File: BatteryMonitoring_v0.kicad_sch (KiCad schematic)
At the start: 33 parts, among them J10 Conn_01x05_Pin, J7 Conn_01x03_Pin, J8 Conn_01x05_Pin, J9 Conn_01x06_Pin, Q6 NPN, SW3 RST_SHUT, SW4 WAKE, U2 PBQ76952PFBT

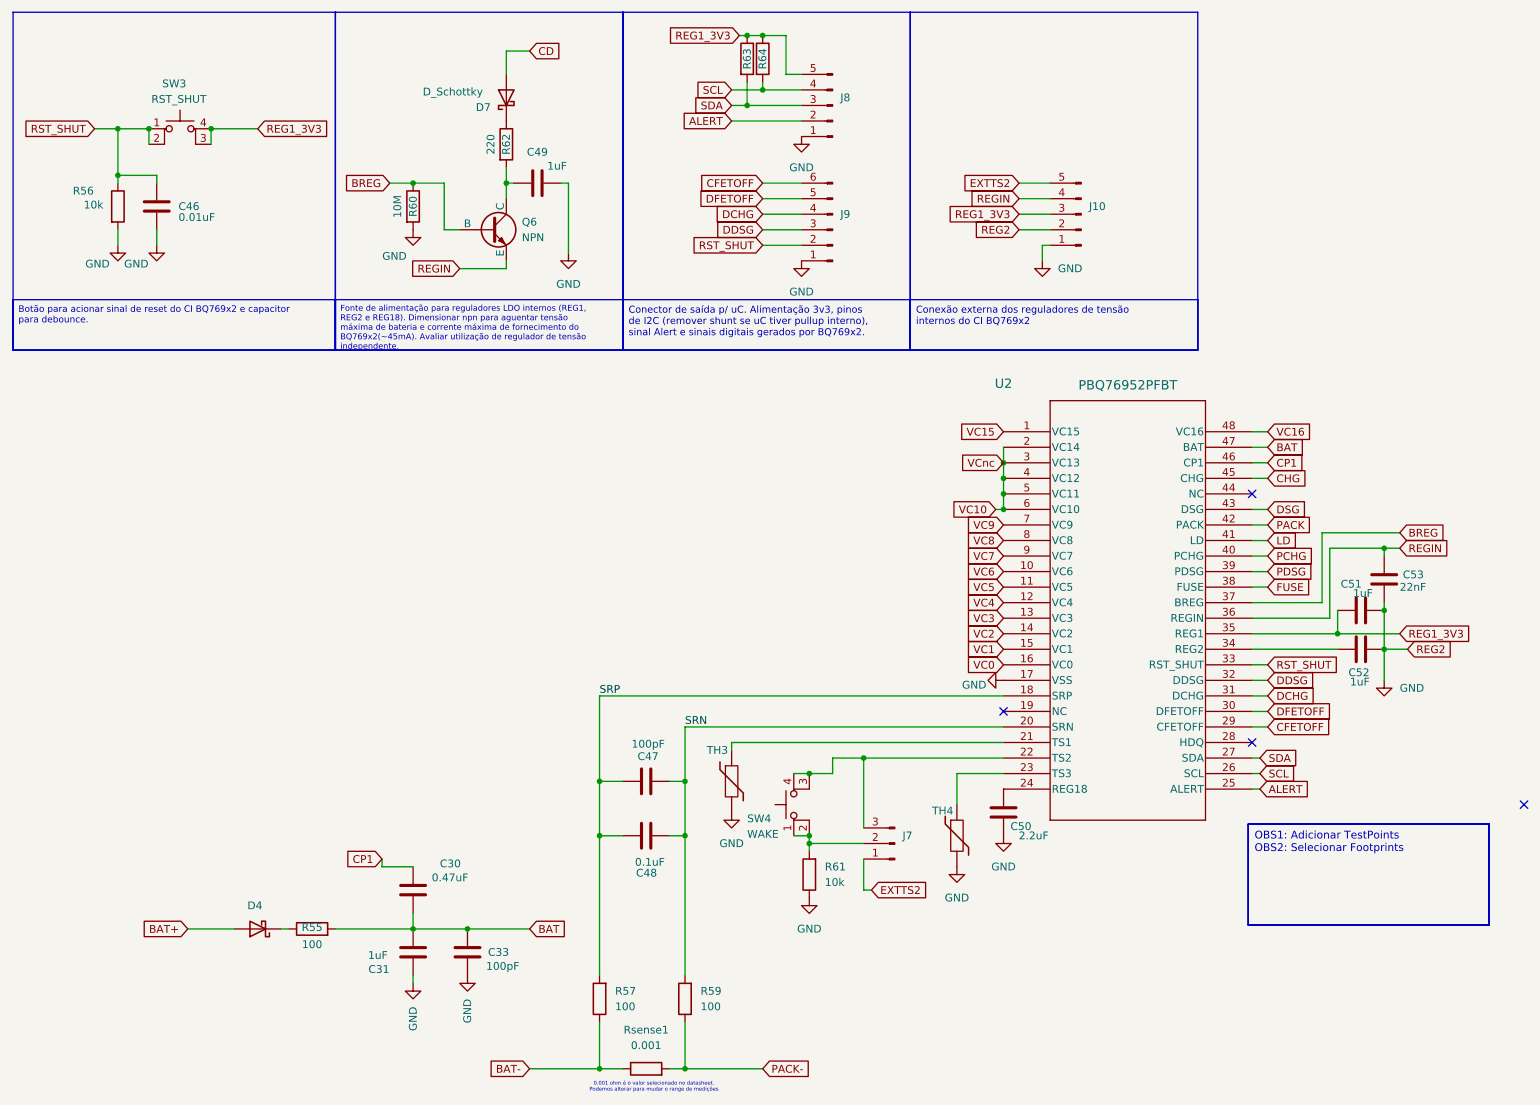
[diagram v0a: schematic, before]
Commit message: Inicio do roteamento e posicionamento da PCB
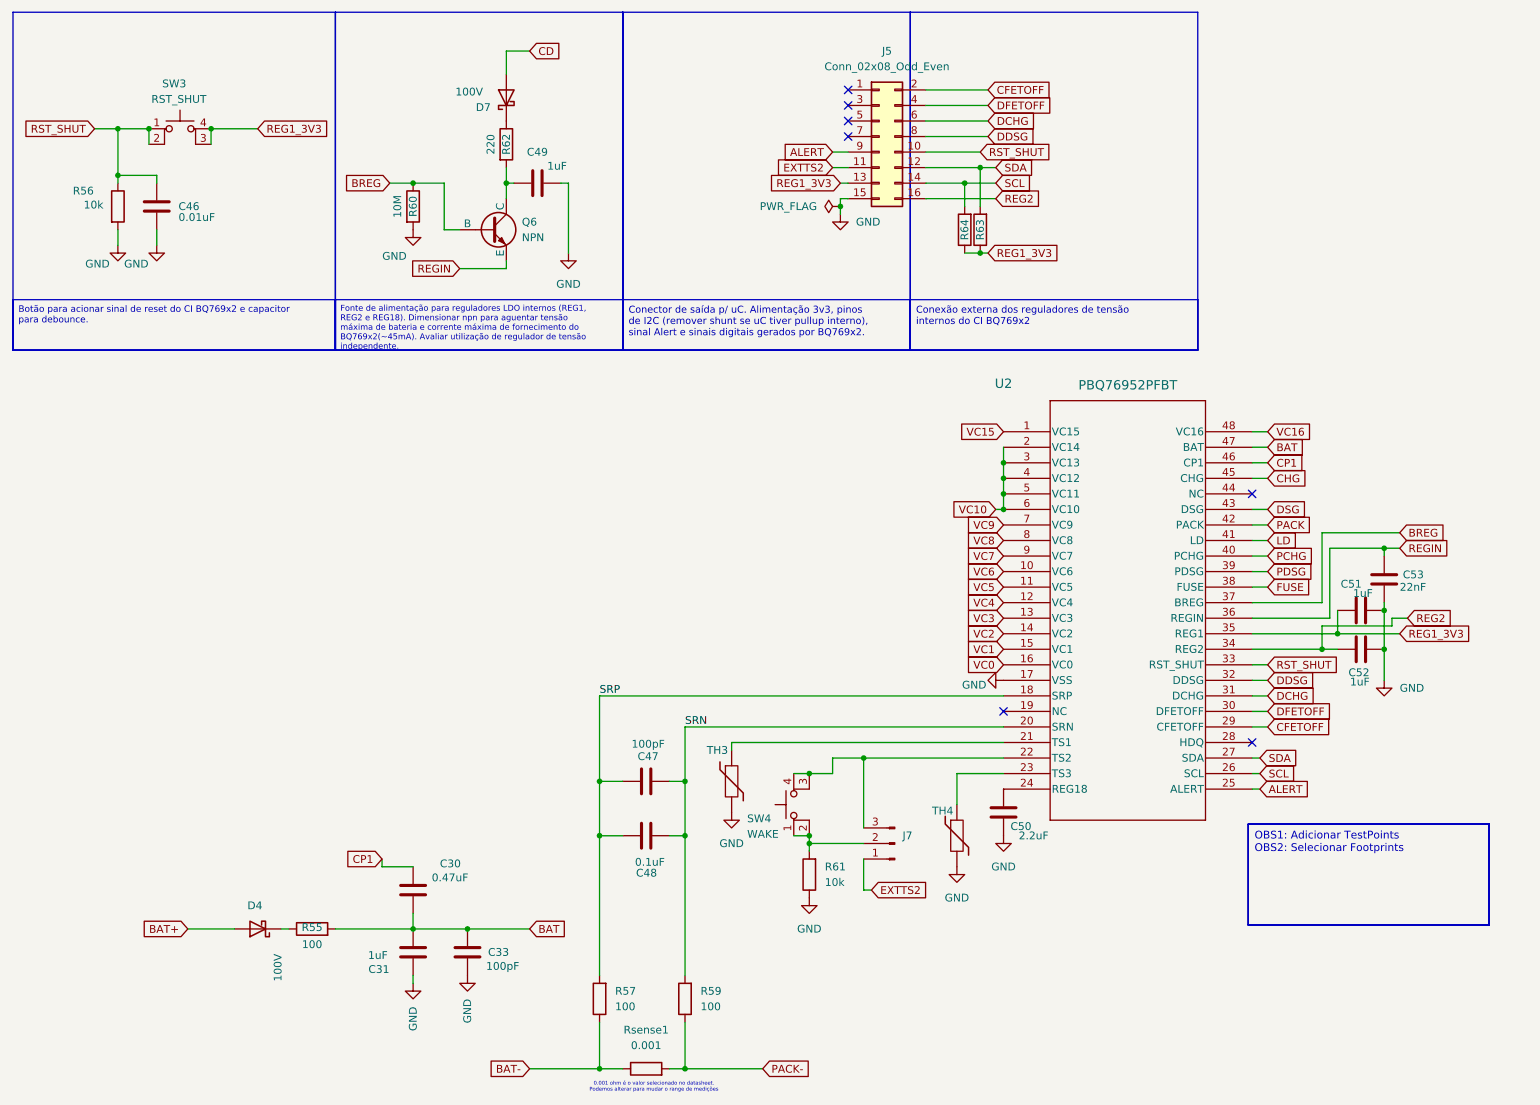
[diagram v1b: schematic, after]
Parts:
- removed J10, J8: Conn_01x05_Pin, Connector_PinHeader_2.54mm:PinHeader_1x05_P2.54mm_Vertical, symbol Connector:Conn_01x05_Pin
- removed J9: Conn_01x06_Pin, Connector_PinHeader_2.54mm:PinHeader_1x06_P2.54mm_Vertical, symbol Connector:Conn_01x06_Pin
- added J5: Conn_02x08_Odd_Even, Connector_PinHeader_2.54mm:PinHeader_2x08_P2.54mm_Vertical, symbol Connector_Generic:Conn_02x08_Odd_Even
- C30, C31, C33, C46, C47, C48, C49, C50, C51, C52, C53: footprint Capacitor_SMD:C_0402_1005Metric_Pad0.74x0.62mm_HandSolder -> Capacitor_SMD:C_1206_3216Metric_Pad1.33x1.80mm_HandSolder
- D4, D7: value D_Schottky -> 100V
- Q6: footprint Package_TO_SOT_SMD:SOT-89-3 -> Package_TO_SOT_THT:TO-92
- R55, R56, R57, R59, R60, R61, R62, R63, R64: footprint Resistor_SMD:R_0402_1005Metric -> Resistor_SMD:R_1206_3216Metric
- TH3, TH4: footprint Footprints:103AT2 -> footprints:103AT2
- U2: footprint Footprints:BQ76952_TEX -> footprints:BQ7692_TEX
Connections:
- net ALERT: now also J5.9 (Pin_9)
- net CFETOFF: now also J5.2 (Pin_2)
- net DCHG: now also J5.6 (Pin_6)
- net DDSG: now also J5.8 (Pin_8)
- net DFETOFF: now also J5.4 (Pin_4)
- net EXTTS2: now also J5.11 (Pin_11)
- net GND: now also J5.15 (Pin_15)
- net REG1_3V3: now also J5.13 (Pin_13)
- net RST_SHUT: now also J5.10 (Pin_10)
- net SCL: now also J5.14 (Pin_14)
- net SDA: now also J5.12 (Pin_12)
- net REG2: now reaches C52.2, U2.34 (REG2)
- net REG2: now also J5.16 (Pin_16)
- no-connect marks 4 -> 7
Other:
- moved on the sheet: R63, R64

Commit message: add Res Shunt e atualiza para Kicad 9.0
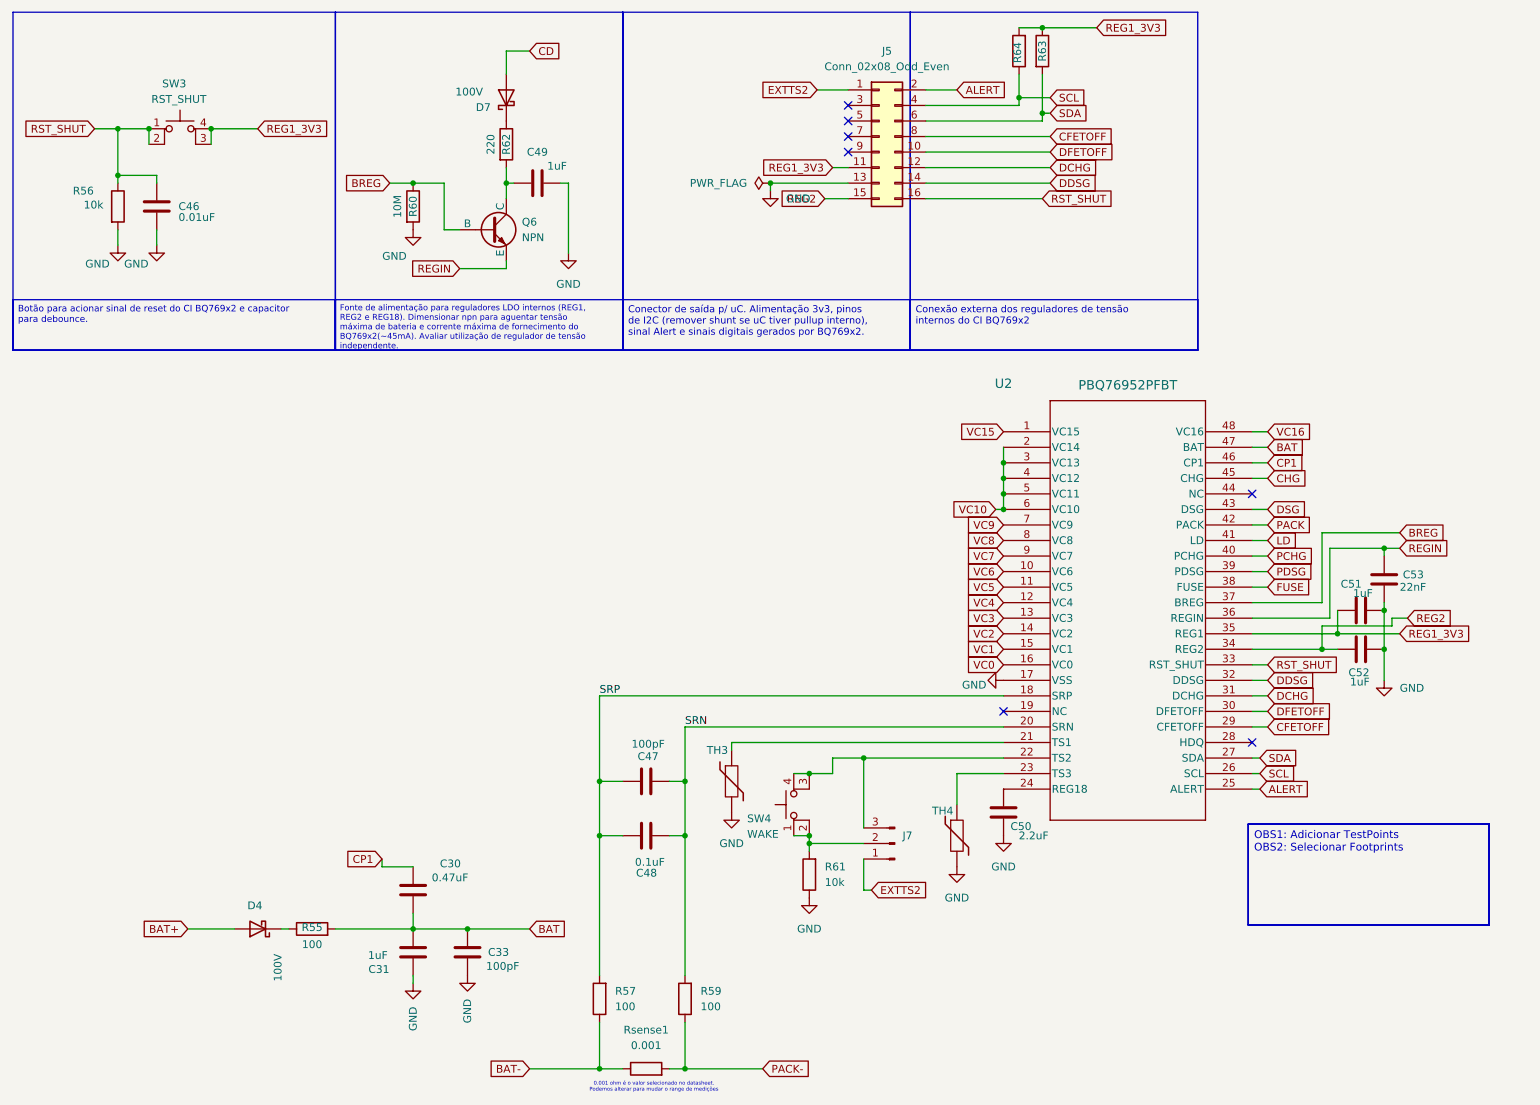
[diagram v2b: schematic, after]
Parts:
- Rsense1: footprint Resistor_SMD:R_0402_1005Metric -> footprints:S200-75
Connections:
- net ALERT: now also J5.2 (Pin_2); no longer J5.9 (Pin_9)
- net CFETOFF: now also J5.8 (Pin_8); no longer J5.2 (Pin_2)
- net DCHG: now also J5.12 (Pin_12); no longer J5.6 (Pin_6)
- net DDSG: now also J5.14 (Pin_14); no longer J5.8 (Pin_8)
- net DFETOFF: now also J5.10 (Pin_10); no longer J5.4 (Pin_4)
- net EXTTS2: now also J5.1 (Pin_1); no longer J5.11 (Pin_11)
- net GND: now also J5.13 (Pin_13); no longer J5.15 (Pin_15)
- net REG1_3V3: now also J5.11 (Pin_11), R64.2; no longer J5.13 (Pin_13), R64.1
- net REG2: now also J5.15 (Pin_15); no longer J5.16 (Pin_16)
- net RST_SHUT: now also J5.16 (Pin_16); no longer J5.10 (Pin_10)
- net SCL: now also J5.4 (Pin_4), R64.1; no longer J5.14 (Pin_14), R64.2
- net SDA: now also J5.6 (Pin_6); no longer J5.12 (Pin_12)
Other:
- moved on the sheet: R63, R64

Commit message: Troca trilhas por regiões
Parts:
- Rsense1: footprint footprints:S200-75 -> footprints:S200_75
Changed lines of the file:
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@@
 			)
 		)
-		(property "Footprint" "footprints:S200-75"
+		(property "Footprint" "footprints:S200_75"
 			(at 143.51 187.198 90)
 			(effects

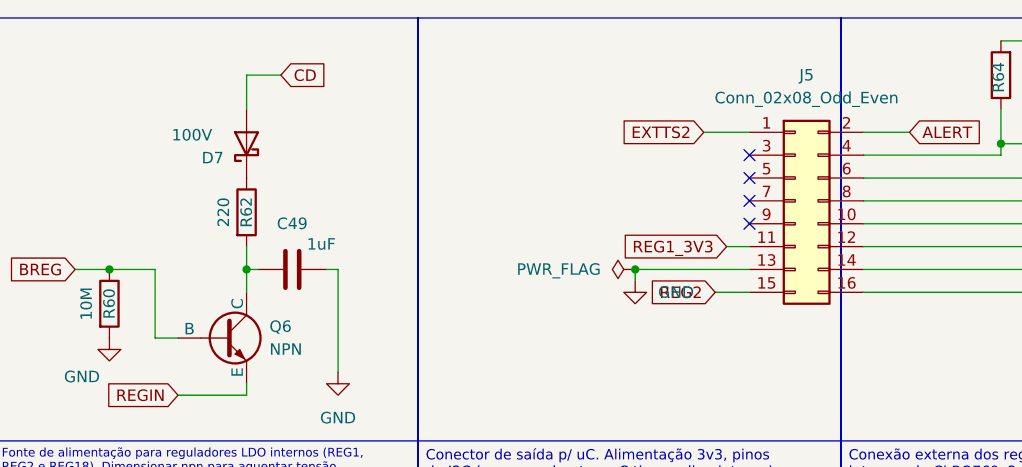
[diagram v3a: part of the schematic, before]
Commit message: Layout com footprints dos componentes da lista
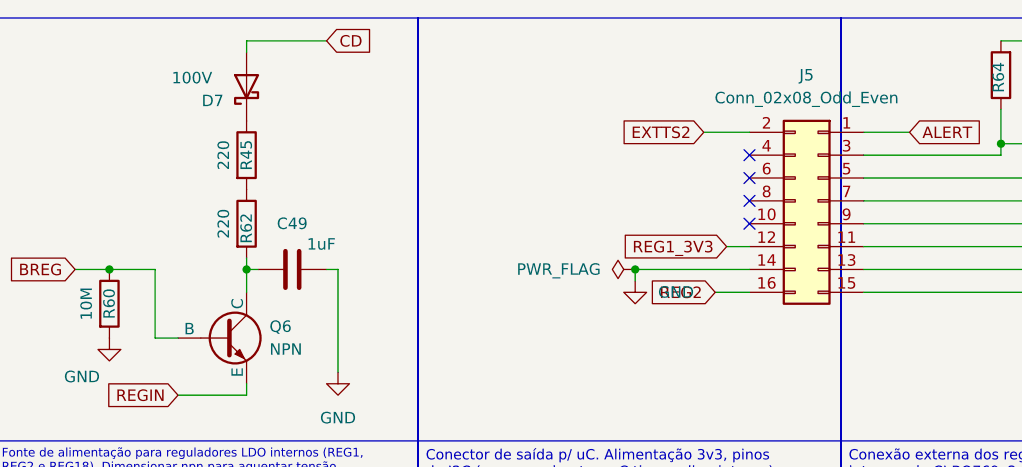
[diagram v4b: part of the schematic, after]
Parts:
- added R45: 220, Resistor_SMD:R_1206_3216Metric, symbol Device:R
- C30: Manufacturer_Part_Number (none) -> CL31B474KBHNNNE
- C31, C49, C51, C52: Manufacturer_Part_Number (none) -> CL31B105KBHNNNE
- C33, C47: Manufacturer_Part_Number (none) -> VPDD102W101K1GV001E
- C46: Manufacturer_Part_Number (none) -> 1206PC103KAT2A
- C48: Manufacturer_Part_Number (none) -> C1206C104K5RACTU
- C50: Manufacturer_Part_Number (none) -> CL31B225KBHNNNE
- C53: Manufacturer_Part_Number (none) -> CC1206JRNPO9BN223
- D4, D7: Manufacturer_Part_Number (none) -> BAT46W-7-F
- J5: footprint Connector_PinHeader_2.54mm:PinHeader_2x08_P2.54mm_Vertical -> footprints:CONN16_SBH11-PBPC-D08-ST-BK_SUL; Manufacturer_Part_Number (none) -> SBH11-PBPC-D08-ST-BK
- J7: Manufacturer_Part_Number (none) -> 2011-1X03G00SB-1
- Q6: Manufacturer_Part_Number (none) -> 2N5830
- R55, R57, R59: Manufacturer_Part_Number (none) -> RC1206FR-07100RL
- R56, R61: Manufacturer_Part_Number (none) -> ERJ-8GEYJ103V
- R60: Manufacturer_Part_Number (none) -> HV732BTTD1005F
- R62: Manufacturer_Part_Number (none) -> CRCW2512220RJNEG
- R63, R64: value R -> 20; Manufacturer_Part_Number (none) -> RC1206FR-0720RL
- SW3: footprint Button_Switch_SMD:SW_MEC_5GSH9 -> footprints:SMT_FS; Manufacturer_Part_Number (none) -> PTS526SM15SMTR2 LFS
- SW4: footprint Button_Switch_SMD:SW_MEC_5GSH9 -> footprints:SMT_FS; Manufacturer_Part_Number (none) -> PTS526SK15SMTR2 LFS
- TH3, TH4: Manufacturer_Part_Number (none) -> 103AT-2
- U2: Manufacturer_Part_Number (none) -> BQ7695202PFBR
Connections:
- net ALERT: now also J5.1 (Pin_1); no longer J5.2 (Pin_2)
- net CFETOFF: now also J5.7 (Pin_7); no longer J5.8 (Pin_8)
- net DCHG: now also J5.11 (Pin_11); no longer J5.12 (Pin_12)
- net DDSG: now also J5.13 (Pin_13); no longer J5.14 (Pin_14)
- net DFETOFF: now also J5.9 (Pin_9); no longer J5.10 (Pin_10)
- net EXTTS2: now also J5.2 (Pin_2); no longer J5.1 (Pin_1)
- net GND: now also J5.14 (Pin_14); no longer J5.13 (Pin_13)
- net REG1_3V3: now also J5.12 (Pin_12); no longer J5.11 (Pin_11)
- net REG2: now also J5.16 (Pin_16); no longer J5.15 (Pin_15)
- net RST_SHUT: now also J5.15 (Pin_15); no longer J5.16 (Pin_16)
- net SCL: now also J5.3 (Pin_3); no longer J5.4 (Pin_4)
- net SDA: now also J5.5 (Pin_5); no longer J5.6 (Pin_6)
- net at D7.1 (K): now also R45.1; no longer R62.1
- new net: R45.2, R62.1
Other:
- moved on the sheet: D7, R62
